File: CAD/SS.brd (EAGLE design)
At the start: 77 x 99.7 mm, 100 parts, among them Q1 SN74AHC-NOR, Q2 UMD5N, Q4 SN74AHC-AND, Q5 BFP460, Q6 TCR1HF50, Q7 NCP553, T1 MMBTRA104SS, X1 ANTENNA, X2 RADIO, X3 INP, X4 AMP-O, X5 BPF-O

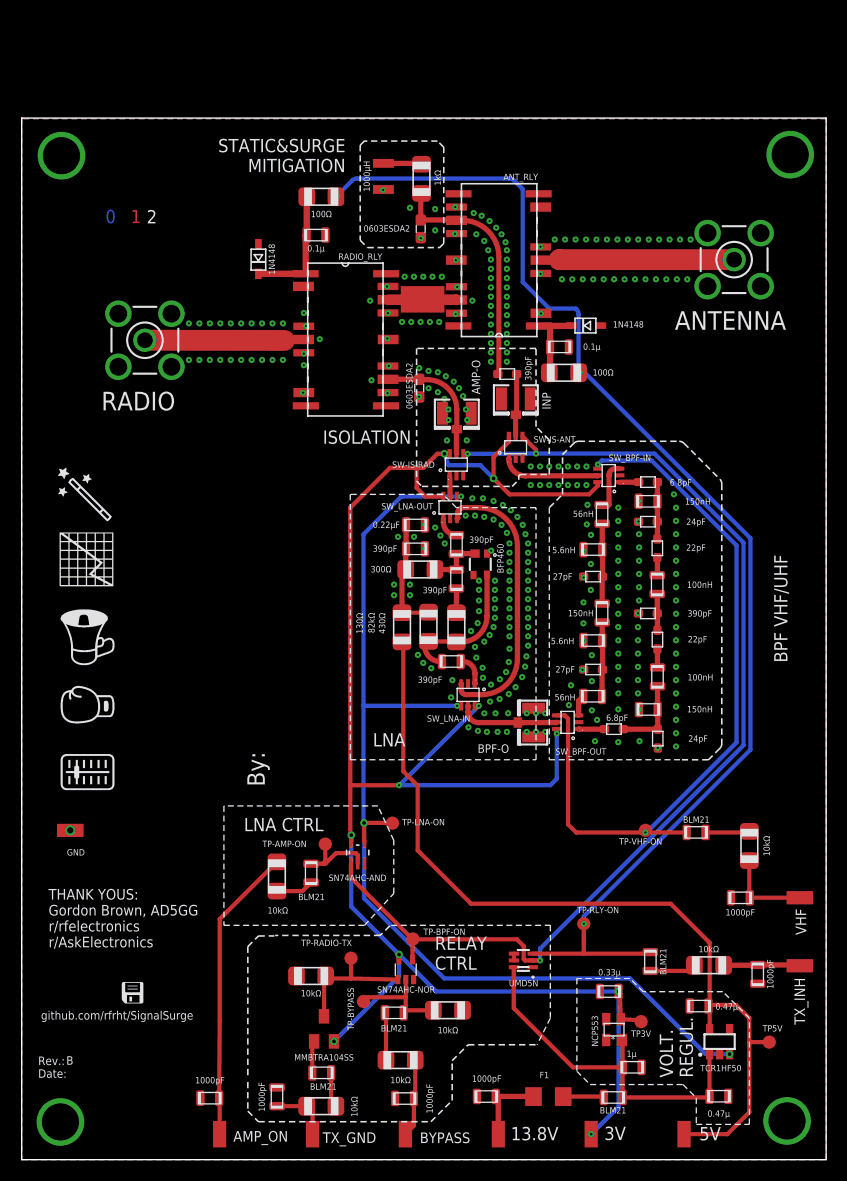
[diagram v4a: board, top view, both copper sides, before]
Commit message: Revision B updates
- Added a detachable board (taking advantage of the spare board real estate) that fits a RTL-SDR Bandpass filter.
- Minor signal and label revisions, routing
- Better labeling for signal I/O by adding expected voltages, improved semiotics
- Tentatively final.
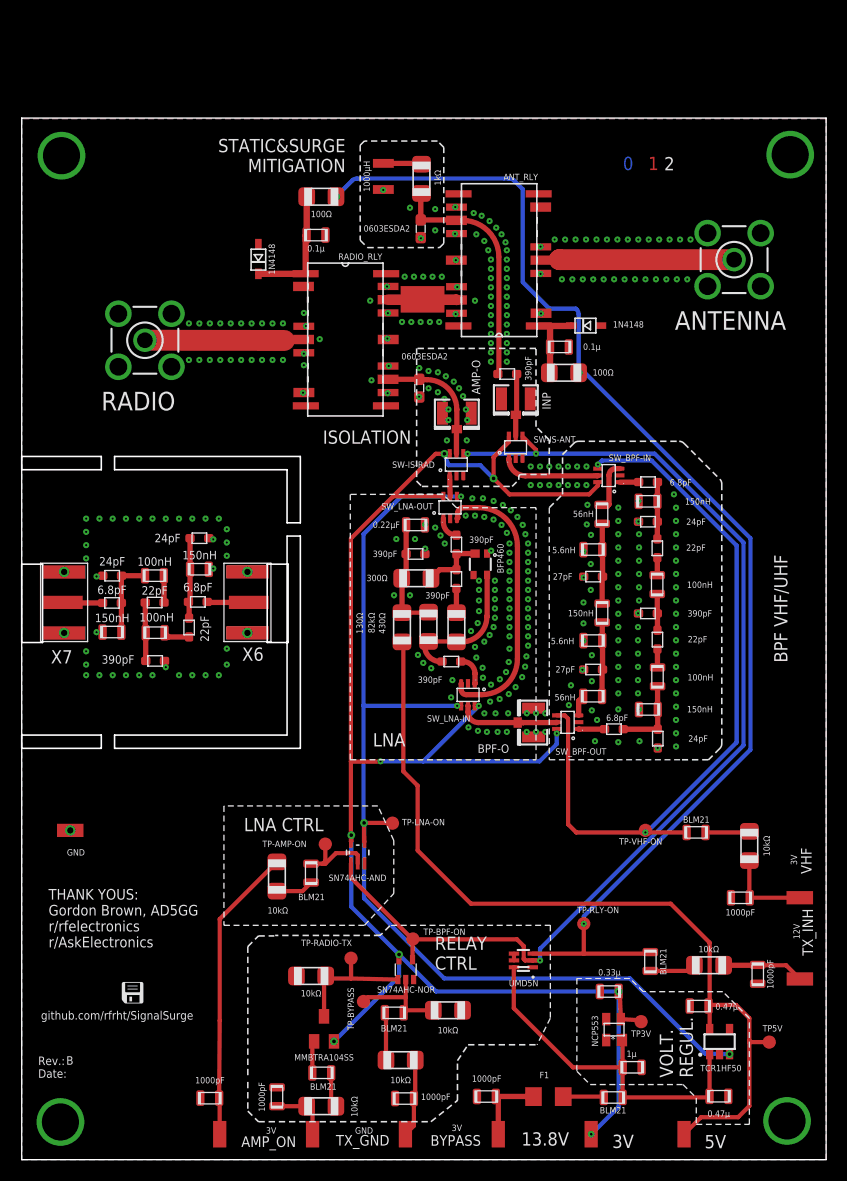
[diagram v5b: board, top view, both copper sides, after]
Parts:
- added C28, C34: 6.8pF, aarf:GRM18
- added C29, C33: 24pF, aarf:GRM18
- added C30, C32: 22pF, aarf:GRM18
- added C31: 390pF, aarf:GRM18
- added L12, L13: 100nH, aarf:0805
- added L14, L5: 150nH, aarf:0805
- added X6, X7: (no value), aarf:SMA-EDGE
- C10, C12, C8, C9: device aarf:0805 -> aarf:GRM18
- moved TX_INH 1.27 mm to (74.5, 17.3)
- moved R3 0.92 mm to (37.8, 55.7)
- moved C10 0.50 mm to (37.7, 58.0)
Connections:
- net RELAY-TO-RELAY_BYPASS renamed RELAY-TO-RELAY_RF
- new net N$18: C28.P$1, C29.P$1, C30.P$2, L5.P$2
- new net N$20: C30.P$1, L12.P$1
- new net N$21: C31.P$1, C32.P$1, L12.P$2
- new net N$23: C33.P$1, C34.P$1, L13.P$2, L14.P$1
- new net N$25: C32.P$2, L13.P$1
- new net VHF-IN1: C28.P$2, X6.P$3
- new net VHF-OUT1: C34.P$2, X7.P$3
- net GND: now also C29.P$2, C31.P$2, C33.P$2, L14.P$2, L5.P$1, X6.P$1, X6.P$2, X6.P$4, X6.P$5, X6.P$6, X6.P$7, X7.P$1, X7.P$2, X7.P$4, X7.P$5, X7.P$6, X7.P$7
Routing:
- net N$18: track 0.00 -> 7.77 mm
- net N$23: track 0.00 -> 7.65 mm
- net 3V: track 173.0 -> 165.6 mm
- net N$21: track 0.00 -> 5.61 mm
- net VHF-IN1: track 0.00 -> 3.99 mm
- net VHF-OUT1: track 0.00 -> 3.83 mm
- net N$25: track 0.00 -> 2.58 mm
- net N$20: track 0.00 -> 2.52 mm
- net LNA-OUT: track 5.37 -> 6.08 mm
- net N$26: track 7.34 -> 7.89 mm
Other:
- outline, holes or cut-outs redrawn
- board text added: "12V"
- board text added: "144 MHz Bandpass filter"
- board text added: "3V"
- board text added: "All flaws by: PY2RAF"
- board text added: "FILTER"
- board text added: "GND"

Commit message: Minor board fixes
- Removed some vias that can be problematic around RF switches
- Fixed silkscreen issues on I/O pads
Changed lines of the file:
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@@
 <drawing>
 <settings>
-<setting alwaysvectorfont="yes"/>
+<setting alwaysvectorfont="no"/>
 <setting verticaltext="up"/>
 </settings>
@@
 <wire x1="75.365" y1="18.366" x2="75.746" y2="18.747" width="0.254" layer="29"/>
 <wire x1="75.746" y1="18.747" x2="75.365" y2="19.128" width="0.254" layer="29"/>
-<wire x1="47.017" y1="2.694" x2="47.017" y2="1.297" width="0.254" layer="29"/>
-<wire x1="47.017" y1="1.297" x2="47.398" y2="1.678" width="0.254" layer="29"/>
-<wire x1="47.017" y1="1.297" x2="46.636" y2="1.678" width="0.254" layer="29"/>
+<wire x1="46.963" y1="1.37" x2="46.963" y2="2.767" width="0.254" layer="29"/>
+<wire x1="46.963" y1="2.767" x2="46.582" y2="2.386" width="0.254" layer="29"/>
+<wire x1="46.963" y1="2.767" x2="47.344" y2="2.386" width="0.254" layer="29"/>
 <wire x1="55.907" y1="2.694" x2="55.907" y2="1.297" width="0.254" layer="29"/>
 <wire x1="55.907" y1="1.297" x2="56.288" y2="1.678" width="0.254" layer="29"/>
@@
 <rectangle x1="33.02" y1="29.718" x2="33.274" y2="31.242" layer="41"/>
 <text x="73.914" y="28.702" size="0.6096" layer="21" font="vector" rot="R90" align="center">3V</text>
-<text x="74.168" y="21.844" size="0.6096" layer="21" font="vector" rot="R90" align="center">12V</text>
+<text x="73.914" y="21.844" size="0.6096" layer="21" font="vector" rot="R90" align="center">12V</text>
 <text x="41.656" y="3.048" size="0.6096" layer="21" font="vector" rot="R180" align="center">3V</text>
 <text x="23.876" y="2.794" size="0.6096" layer="21" font="vector" rot="R180" align="center">3V</text>
-<text x="32.766" y="2.794" size="0.6096" layer="21" font="vector" rot="R180" align="center">GND</text>
+<text x="32.766" y="3.048" size="0.6096" layer="21" font="vector" rot="R180" align="center">GND</text>
 </plain>
 <attributes>
@@
 </element>
 <element name="TX_INH" library="wirepad" library_urn="urn:adsk.eagle:library:412" package="SMD1,27-2,54" package3d_urn="urn:adsk.eagle:package:30839/1" value="TX INH" x="74.484" y="17.295" smashed="yes" rot="R270">
-<attribute name="NAME" x="75.235" y="21.776" size="1.016" layer="21" font="vector" rot="R270" align="center"/>
+<attribute name="NAME" x="74.981" y="21.776" size="1.016" layer="21" font="vector" rot="R270" align="center"/>
 <attribute name="SPICEPREFIX" value="X" x="74.484" y="17.295" size="1.778" layer="27" rot="R270" display="off"/>
 </element>
@@
 </element>
 <element name="5V" library="wirepad" library_urn="urn:adsk.eagle:library:412" package="SMD1,27-2,54" package3d_urn="urn:adsk.eagle:package:30839/1" value="5V" x="63.4" y="2.44" smashed="yes">
-<attribute name="NAME" x="66.395" y="1.726" size="1.27" layer="21" font="vector" rot="R180" align="center"/>
+<attribute name="NAME" x="66.649" y="1.98" size="1.27" layer="21" font="vector" rot="R180" align="center"/>
 <attribute name="VALUE" x="119.28" y="2.44" size="0.0254" layer="27"/>
 </element>
 <element name="3V" library="wirepad" library_urn="urn:adsk.eagle:library:412" package="SMD1,27-2,54" package3d_urn="urn:adsk.eagle:package:30839/1" value="3V" x="54.51" y="2.44" smashed="yes">
-<attribute name="NAME" x="57.559" y="1.753" size="1.27" layer="21" font="vector" rot="R180" align="center"/>
+<attribute name="NAME" x="57.813" y="2.007" size="1.27" layer="21" font="vector" rot="R180" align="center"/>
 <attribute name="VALUE" x="123.09" y="2.44" size="0.0254" layer="27"/>
 </element>
@@
 <via x="54.472" y="57.016" extent="1-16" drill="0.2"/>
 <via x="53.772" y="58.222" extent="1-16" drill="0.2"/>
-<via x="50.119" y="40.947" extent="1-16" drill="0.2"/>
-<via x="49.23" y="40.947" extent="1-16" drill="0.2"/>
+<via x="49.068" y="40.587" extent="1-16" drill="0.2"/>
 <via x="46.436" y="40.947" extent="1-16" drill="0.2"/>
 <via x="45.547" y="40.947" extent="1-16" drill="0.2"/>
@@
 <via x="46.359" y="46.676" extent="1-16" drill="0.2"/>
 <via x="47.904" y="46.189" extent="1-16" drill="0.2"/>
-<via x="48.341" y="40.947" extent="1-16" drill="0.2"/>
 <via x="44.285" y="42.725" extent="1-16" drill="0.2"/>
 <via x="45.354" y="42.725" extent="1-16" drill="0.2"/>
 <via x="46.563" y="42.725" extent="1-16" drill="0.2"/>
-<via x="48.341" y="42.725" extent="1-16" drill="0.2"/>
-<via x="50.119" y="42.725" extent="1-16" drill="0.2"/>
-<via x="49.23" y="42.725" extent="1-16" drill="0.2"/>
+<via x="49.103" y="43.233" extent="1-16" drill="0.2"/>
 <via x="54.056" y="64.569" extent="1-16" drill="0.2"/>
 <via x="53.167" y="64.569" extent="1-16" drill="0.2"/>
@@
 <via x="45.166" y="61.267" extent="1-16" drill="0.2"/>
 <via x="44.277" y="61.521" extent="1-16" drill="0.2"/>
-<via x="43.388" y="61.648" extent="1-16" drill="0.2"/>
 <via x="46.055" y="62.664" extent="1-16" drill="0.2"/>
 <via x="46.817" y="62.156" extent="1-16" drill="0.2"/>
@@
 <via x="45.293" y="53.647" extent="1-16" drill="0.2"/>
 <via x="45.293" y="54.536" extent="1-16" drill="0.2"/>
-<via x="45.293" y="55.425" extent="1-16" drill="0.2"/>
+<via x="45.547" y="55.425" extent="1-16" drill="0.2"/>
 <via x="43.007" y="50.599" extent="1-16" drill="0.2"/>
 <via x="43.769" y="52.504" extent="1-16" drill="0.2"/>
@@
 <via x="45.166" y="63.045" extent="1-16" drill="0.2"/>
 <via x="43.134" y="63.299" extent="1-16" drill="0.2"/>
-<via x="42.499" y="61.648" extent="1-16" drill="0.2"/>
+<via x="43.007" y="61.648" extent="1-16" drill="0.2"/>
 <via x="33.482" y="74.602" extent="1-16" drill="0.2"/>
 <via x="33.355" y="82.222" extent="1-16" drill="0.2"/>
@@
 <via x="45.747" y="44.093" extent="1-16" drill="0.2"/>
 <via x="37.927" y="48.313" extent="1-16" drill="0.2"/>
-<via x="41.229" y="45.9" extent="1-16" drill="0.2"/>
+<via x="40.975" y="45.9" extent="1-16" drill="0.2"/>
 <via x="38.435" y="47.551" extent="1-16" drill="0.2"/>
 <via x="41.102" y="44.249" extent="1-16" drill="0.2"/>
@@
 <via x="39.197" y="47.043" extent="1-16" drill="0.2"/>
 <via x="43.515" y="48.059" extent="1-16" drill="0.2"/>
-<via x="44.116" y="47.083" extent="1-16" drill="0.2"/>
+<via x="44.116" y="46.575" extent="1-16" drill="0.2"/>
 <via x="73.26" y="3.71" extent="1-16" drill="3.556"/>
 <via x="3.71" y="3.61" extent="1-16" drill="3.556"/>
@@
 <via x="44.912" y="80.834" extent="1-16" drill="0.2"/>
 <via x="46.442" y="80.834" extent="1-16" drill="0.2"/>
-<via x="44.146" y="46.133" extent="1-16" drill="0.2"/>
 <contactref element="C31" pad="P$2"/>
 <contactref element="C29" pad="P$2"/>

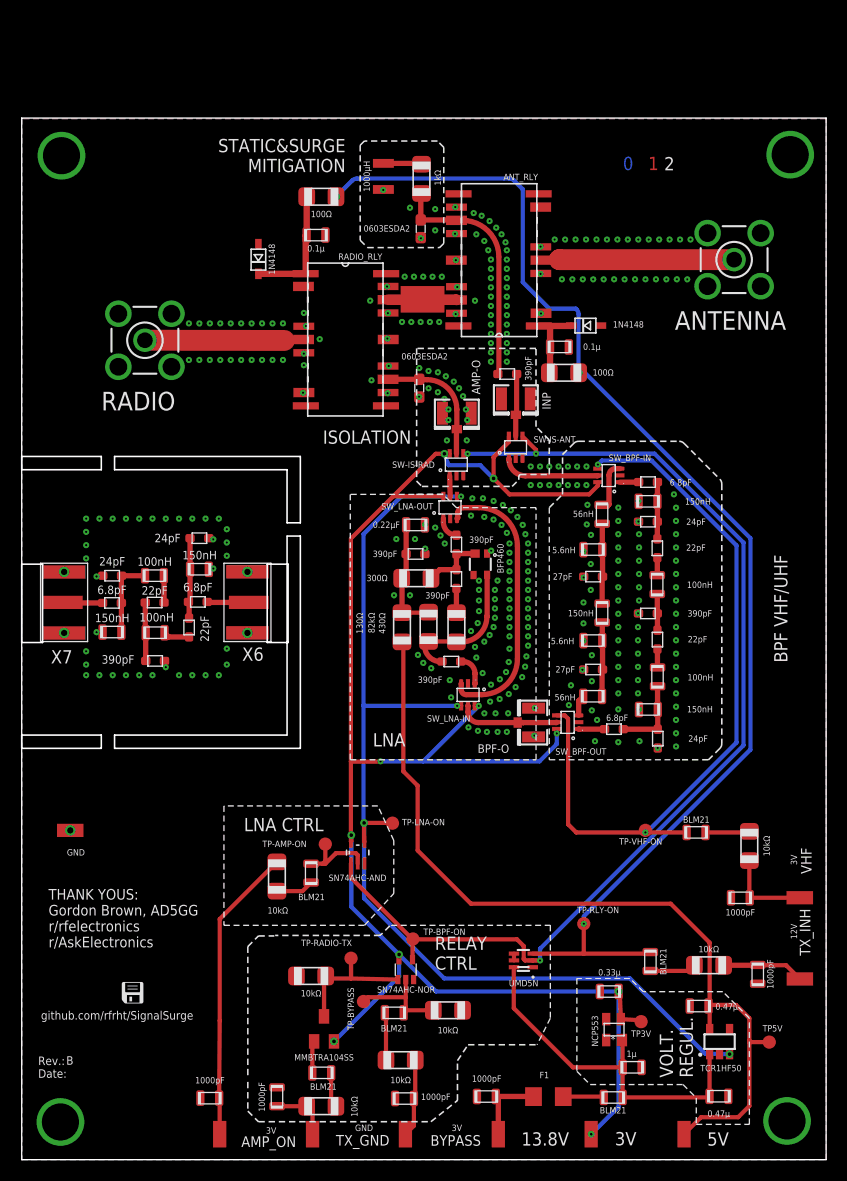
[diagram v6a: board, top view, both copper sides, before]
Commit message: Board: Changed pads to jumpers
Why I didn't do it before, doh. Pads are... Complicated.

Also:

- Changed the silk of the fuse (now with value)
- Relabeled the region around the jumper
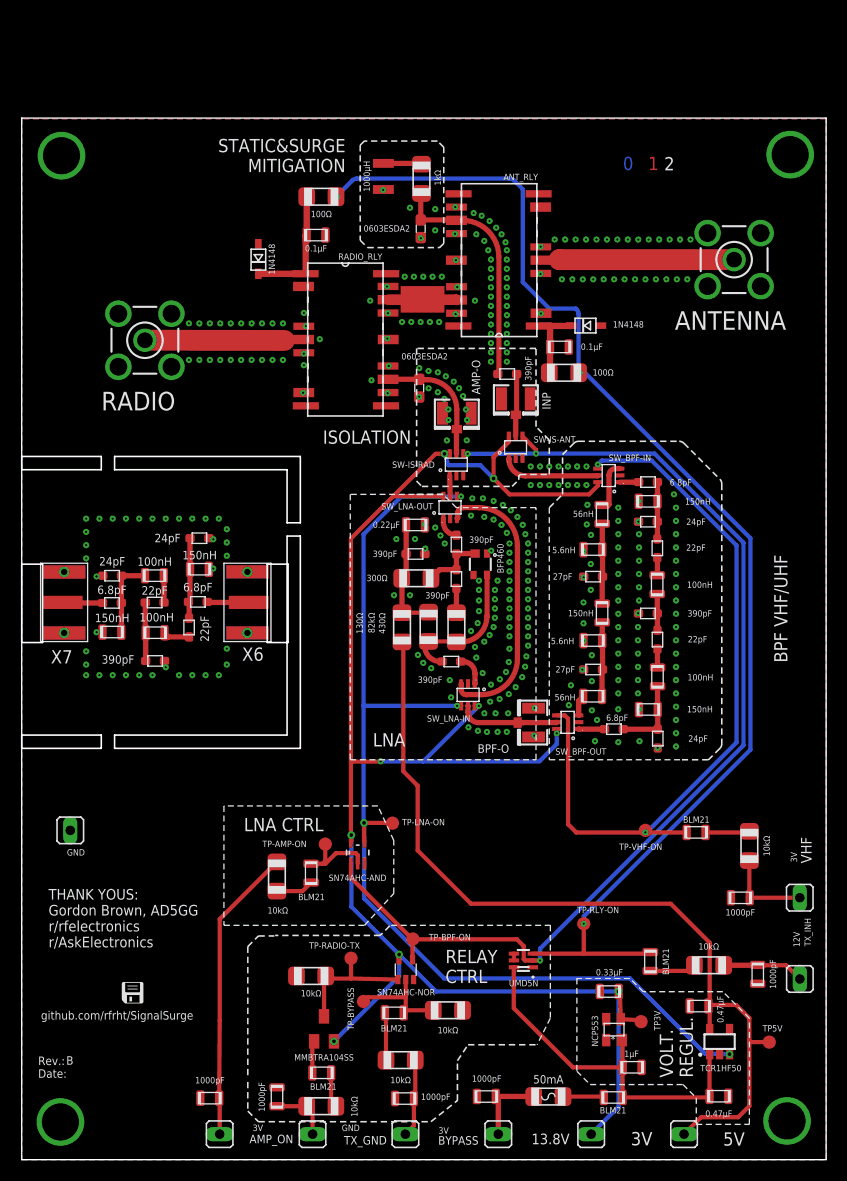
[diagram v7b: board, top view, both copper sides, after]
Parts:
- 13.8V, 3V, 5V, AMP_ON, BYPASS, GND, TX_GND, TX_INH, VHF: device wirepad:SMD1,27-2,54 -> aarf:JUMPER1
- C17, C18: value 0.1µ -> 0.1µF
- C21, C22: value 0.47µ -> 0.47µF
- C23: value 1µ -> 1µF
- C24: value 0.33µ -> 0.33µF
- F1: value 1231 -> 50mA; device adafruit:R1206 -> aarf:FUSE-1206
